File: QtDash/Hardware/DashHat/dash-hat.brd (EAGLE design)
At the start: 120.9 x 74.9 mm, 169 parts, among them IC1 LMV614, IC10 MAX9924, IC11 ZXTR2105FQ, IC2 MCP3X083008, IC3 MCP23017SS, IC4 LM358D, IC5 IL300, IC6 TSV912D, IC7 IL300, IC8 TSV912D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

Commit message: bugfix/analog-12v-input-linearity-issues: 	- added reference update after every reading -- probably not necessary 	- changed IL300 circuit values to increase drive current and opamp output voltage to deal with non-linearities in lower voltages
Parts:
- R53, R59: value 499k 1% -> 100k 1%
- R55, R61: value 10R -> 270 1%
- R56, R62: value 100k -> 20k 1%
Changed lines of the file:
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@@
 <grid distance="5" unitdist="mil" unit="mil" style="lines" multiple="1" display="yes" altdistance="1" altunitdist="mil" altunit="mil"/>
 <layers>
-<layer number="1" name="Top" color="4" fill="1" visible="yes" active="yes"/>
-<layer number="2" name="Route2" color="1" fill="3" visible="yes" active="yes"/>
+<layer number="1" name="Top" color="4" fill="1" visible="no" active="yes"/>
+<layer number="2" name="Route2" color="1" fill="3" visible="no" active="yes"/>
 <layer number="3" name="Route3" color="4" fill="3" visible="no" active="no"/>
 <layer number="4" name="Route4" color="1" fill="4" visible="no" active="no"/>
@@
 <layer number="13" name="Route13" color="4" fill="5" visible="no" active="no"/>
 <layer number="14" name="Route14" color="1" fill="6" visible="no" active="no"/>
-<layer number="15" name="Route15" color="4" fill="6" visible="yes" active="yes"/>
+<layer number="15" name="Route15" color="4" fill="6" visible="no" active="yes"/>
 <layer number="16" name="Bottom" color="9" fill="1" visible="yes" active="yes"/>
 <layer number="17" name="Pads" color="2" fill="1" visible="yes" active="yes"/>
@@
 <layer number="19" name="Unrouted" color="6" fill="1" visible="yes" active="yes"/>
 <layer number="20" name="Dimension" color="15" fill="1" visible="yes" active="yes"/>
-<layer number="21" name="tPlace" color="54" fill="1" visible="yes" active="yes"/>
-<layer number="22" name="bPlace" color="54" fill="1" visible="no" active="yes"/>
-<layer number="23" name="tOrigins" color="55" fill="1" visible="yes" active="yes"/>
-<layer number="24" name="bOrigins" color="55" fill="1" visible="no" active="yes"/>
-<layer number="25" name="tNames" color="58" fill="1" visible="yes" active="yes"/>
-<layer number="26" name="bNames" color="58" fill="1" visible="no" active="yes"/>
+<layer number="21" name="tPlace" color="54" fill="1" visible="no" active="yes"/>
+<layer number="22" name="bPlace" color="54" fill="1" visible="yes" active="yes"/>
+<layer number="23" name="tOrigins" color="55" fill="1" visible="no" active="yes"/>
+<layer number="24" name="bOrigins" color="55" fill="1" visible="yes" active="yes"/>
+<layer number="25" name="tNames" color="58" fill="1" visible="no" active="yes"/>
+<layer number="26" name="bNames" color="58" fill="1" visible="yes" active="yes"/>
 <layer number="27" name="tValues" color="7" fill="1" visible="no" active="yes"/>
-<layer number="28" name="bValues" color="7" fill="1" visible="no" active="yes"/>
-<layer number="29" name="tStop" color="7" fill="3" visible="yes" active="yes"/>
-<layer number="30" name="bStop" color="7" fill="6" visible="no" active="yes"/>
-<layer number="31" name="tCream" color="7" fill="4" visible="yes" active="yes"/>
-<layer number="32" name="bCream" color="7" fill="5" visible="no" active="yes"/>
+<layer number="28" name="bValues" color="7" fill="1" visible="yes" active="yes"/>
+<layer number="29" name="tStop" color="7" fill="3" visible="no" active="yes"/>
+<layer number="30" name="bStop" color="7" fill="6" visible="yes" active="yes"/>
+<layer number="31" name="tCream" color="7" fill="4" visible="no" active="yes"/>
+<layer number="32" name="bCream" color="7" fill="5" visible="yes" active="yes"/>
 <layer number="33" name="tFinish" color="6" fill="3" visible="no" active="yes"/>
 <layer number="34" name="bFinish" color="6" fill="6" visible="no" active="yes"/>
@@
 <layer number="37" name="tTest" color="7" fill="1" visible="no" active="yes"/>
 <layer number="38" name="bTest" color="7" fill="1" visible="no" active="yes"/>
-<layer number="39" name="tKeepout" color="4" fill="11" visible="yes" active="yes"/>
-<layer number="40" name="bKeepout" color="1" fill="11" visible="no" active="yes"/>
-<layer number="41" name="tRestrict" color="4" fill="10" visible="yes" active="yes"/>
-<layer number="42" name="bRestrict" color="1" fill="10" visible="no" active="yes"/>
+<layer number="39" name="tKeepout" color="4" fill="11" visible="no" active="yes"/>
+<layer number="40" name="bKeepout" color="1" fill="11" visible="yes" active="yes"/>
+<layer number="41" name="tRestrict" color="4" fill="10" visible="no" active="yes"/>
+<layer number="42" name="bRestrict" color="1" fill="10" visible="yes" active="yes"/>
 <layer number="43" name="vRestrict" color="2" fill="10" visible="yes" active="yes"/>
 <layer number="44" name="Drills" color="7" fill="1" visible="yes" active="yes"/>
@@
 <element name="R57" library="digital_dash" package="0603" value="100R" x="83.312" y="20.574" rot="MR0"/>
 <element name="IC5" library="digital_dash" package="DIL8-SMD" value="IL300" x="62.23" y="14.986" rot="MR0"/>
-<element name="R53" library="digital_dash" package="0603" value="499k 1%" x="69.723" y="10.414" rot="MR90"/>
-<element name="R55" library="digital_dash" package="0603" value="10R" x="70.358" y="16.256" rot="MR0"/>
-<element name="R56" library="digital_dash" package="0603" value="100k" x="52.578" y="18.288" smashed="yes" rot="MR180">
+<element name="R53" library="digital_dash" package="0603" value="100k 1%" x="69.723" y="10.414" rot="MR90"/>
+<element name="R55" library="digital_dash" package="0603" value="270 1%" x="70.358" y="16.256" rot="MR0"/>
+<element name="R56" library="digital_dash" package="0603" value="20k 1%" x="52.578" y="18.288" smashed="yes" rot="MR180">
 <attribute name="NAME" x="50.038" y="18.288" size="0.6096" layer="26" font="vector" ratio="20" rot="MR180" align="bottom-center"/>
-<attribute name="VALUE" x="49.784" y="18.542" size="0.6096" layer="28" font="vector" ratio="20" rot="MR180" align="top-center"/>
+<attribute name="VALUE" value="20k 1%" x="49.784" y="18.542" size="0.6096" layer="28" font="vector" ratio="20" rot="MR180" align="top-center"/>
 </element>
 <element name="IC6" library="digital_dash" package="SO08" value="TSV912D" x="51.308" y="23.368" smashed="yes" rot="MR90">
@@
 <attribute name="VALUE" x="82.55" y="31.242" size="0.6096" layer="28" font="vector" ratio="20" rot="MR0" align="top-center"/>
 </element>
-<element name="R59" library="digital_dash" package="0603" value="499k 1%" x="67.945" y="23.241" smashed="yes" rot="MR90">
+<element name="R59" library="digital_dash" package="0603" value="100k 1%" x="67.945" y="23.241" smashed="yes" rot="MR90">
 <attribute name="NAME" x="68.834" y="23.241" size="0.6096" layer="26" font="vector" ratio="20" rot="MR90" align="bottom-center"/>
-<attribute name="VALUE" value="499k 1%" x="67.183" y="23.241" size="0.6096" layer="28" font="vector" ratio="20" rot="MR90" align="top-center"/>
+<attribute name="VALUE" value="100k 1%" x="67.183" y="23.241" size="0.6096" layer="28" font="vector" ratio="20" rot="MR90" align="top-center"/>
 </element>
 <element name="IC7" library="digital_dash" package="DIL8-SMD" value="IL300" x="62.484" y="29.972" rot="MR0"/>
-<element name="R61" library="digital_dash" package="0603" value="10R" x="70.866" y="31.242" rot="MR0"/>
-<element name="R62" library="digital_dash" package="0603" value="100k" x="51.308" y="28.448" smashed="yes" rot="MR180">
+<element name="R61" library="digital_dash" package="0603" value="270 1%" x="70.866" y="31.242" rot="MR0"/>
+<element name="R62" library="digital_dash" package="0603" value="20k 1%" x="51.308" y="28.448" smashed="yes" rot="MR180">
 <attribute name="NAME" x="48.768" y="28.702" size="0.6096" layer="26" font="vector" ratio="20" rot="MR180" align="bottom-center"/>
-<attribute name="VALUE" x="48.514" y="27.686" size="0.6096" layer="28" font="vector" ratio="20" rot="MR180" align="top-center"/>
+<attribute name="VALUE" value="20k 1%" x="48.514" y="27.686" size="0.6096" layer="28" font="vector" ratio="20" rot="MR180" align="top-center"/>
 </element>
 <element name="IC4" library="digital_dash" package="SO08" value="LM358D" x="77.47" y="22.098" smashed="yes" rot="MR90">

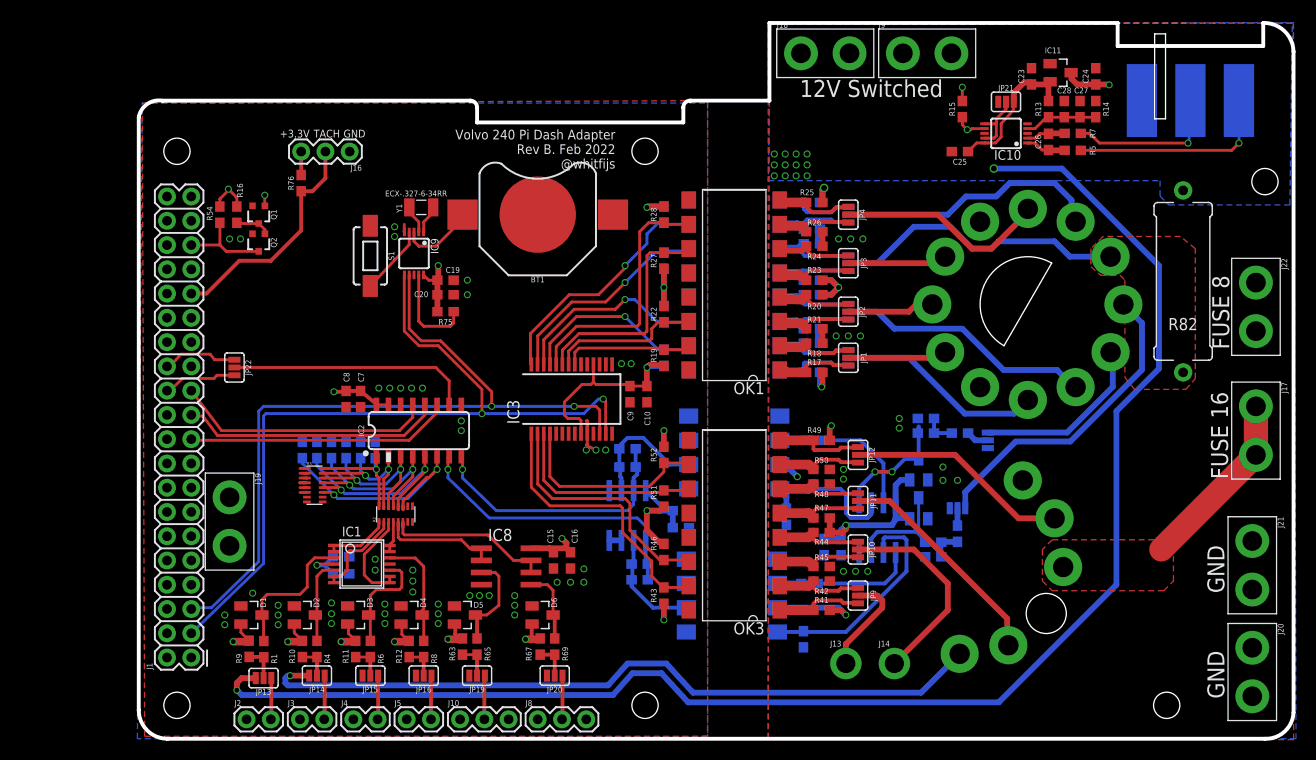
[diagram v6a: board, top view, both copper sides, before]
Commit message: topic/hardware-revc: 	- removed individual pin headers for sensor inputs -- changed to molex 8 pin for now, might be too large
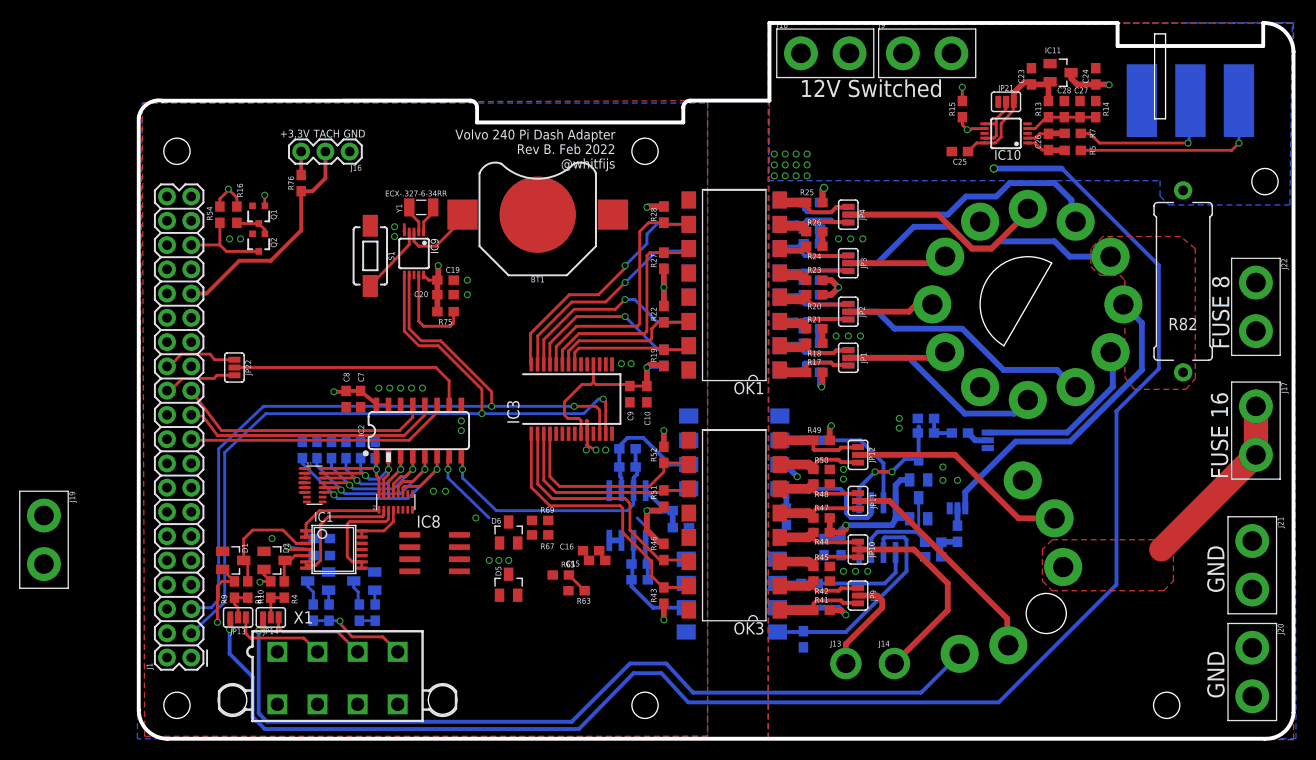
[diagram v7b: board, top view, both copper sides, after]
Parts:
- removed J10, J8: 455-1750-1-ND, SparkFun-Connectors:1X03
- removed J2, J3, J4, J5: (no value), SparkFun-Connectors:1X02
- removed JP15, JP16, JP19, JP20: JUMPER-SMT_3_NO_SILK, SparkFun-Jumpers:SMT-JUMPER_3_NO_SILK
- added X1: 5566-8, con-molex:5566-8
- moved J19 19.5 mm to (-9.78, 20.8)
- moved R69 13.3 mm to (42.2, 22.9), turned to 180 degrees
- moved R63 13.3 mm to (46.0, 15.5), turned to 180 degrees
- moved R67 11.7 mm to (42.2, 21.3), turned to 180 degrees
- moved R65 11.5 mm to (44.3, 17.1), turned to 180 degrees
- moved D6 9.34 mm to (38.9, 21.6), turned to 0 degrees
- moved JP14 7.78 mm to (14.0, 12.7)
- moved R8 7.73 mm to (23.2, 13.2), flipped to the bottom
- moved IC8 7.62 mm to (31.1, 19.4)
- moved R4 7.11 mm to (15.4, 15.6)
- moved R6 7.08 mm to (18.4, 13.2), flipped to the bottom
- moved R10 7.04 mm to (14.0, 15.6)
- moved JP13 6.89 mm to (10.5, 12.7)
- moved D2 6.54 mm to (14.4, 18.7)
- moved R1 6.46 mm to (11.6, 15.6)
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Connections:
- removed net AMBIENT_TEMP: JP20.3
- removed net MAP_SENSOR: JP19.3
- removed net N$30: JP15.2, R11.1, R6.1
- removed net N$31: JP16.2, R12.1, R8.1
- removed net N$34: JP19.2, R63.1, R65.1
- removed net N$37: JP20.2, R67.1, R69.1
- removed net OIL_PRESSURE: JP15.3
- removed net OIL_TEMP: JP16.3
- net 5V: now also X1.1; no longer J10.3, J8.3
- net GND: now also X1.8; no longer J10.1, J2.1, J3.1, J4.1, J5.1, J8.1
- net SENSOR1_IN: now also X1.2; no longer J2.2
- net SENSOR2_IN: now also X1.3; no longer J3.2
- net SENSOR3_IN: now also R11.1, R6.1, X1.4; no longer J4.2, JP15.1
- net SENSOR4_IN: now also R12.1, R8.1, X1.5; no longer J5.2, JP16.1
- net SENSOR5_IN: now also R63.1, R65.1, X1.6; no longer J10.2, JP19.1
- net SENSOR6_IN: now also R67.1, R69.1, X1.7; no longer J8.2, JP20.1
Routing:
- net N$35: track 17.7 -> 0.00 mm
- net SIG_3V3_IN1: track 30.9 -> 15.4 mm
- net 5V: track 32.9 -> 18.4 mm, vias 8 -> 3
- net N$28: track 13.0 -> 0.00 mm
- net FUEL_LVL_SENDER: track 77.9 -> 89.6 mm
- net N$29: track 10.6 -> 0.00 mm
- net N$15: track 11.9 -> 2.70 mm
- net N$11: track 11.5 -> 2.70 mm
- net COOLANT_TEMP_SENSOR: track 165.7 -> 174.3 mm
- net N$36: track 7.76 -> 0.17 mm
- net SENSOR2_IN: track 4.58 -> 10.4 mm
- net SENSOR3_IN: track 4.59 -> 10.4 mm, vias 0 -> 1
- net SENSOR1_IN: track 4.34 -> 9.99 mm
- net SENSOR6_IN: track 4.59 -> 0.00 mm
- net N$7: track 8.95 -> 4.65 mm
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
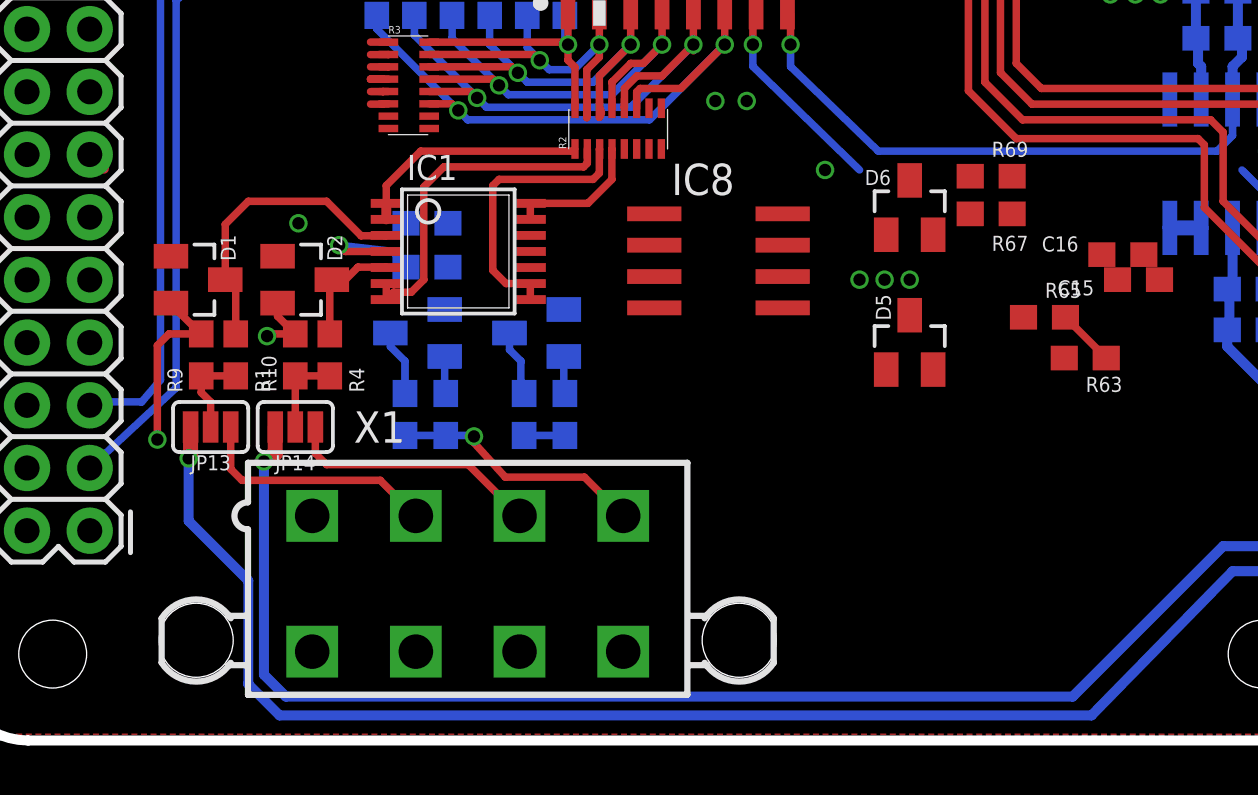
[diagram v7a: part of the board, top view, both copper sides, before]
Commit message: topic/hardware-revc: 	- replaced larger molex connector smaller molex connector
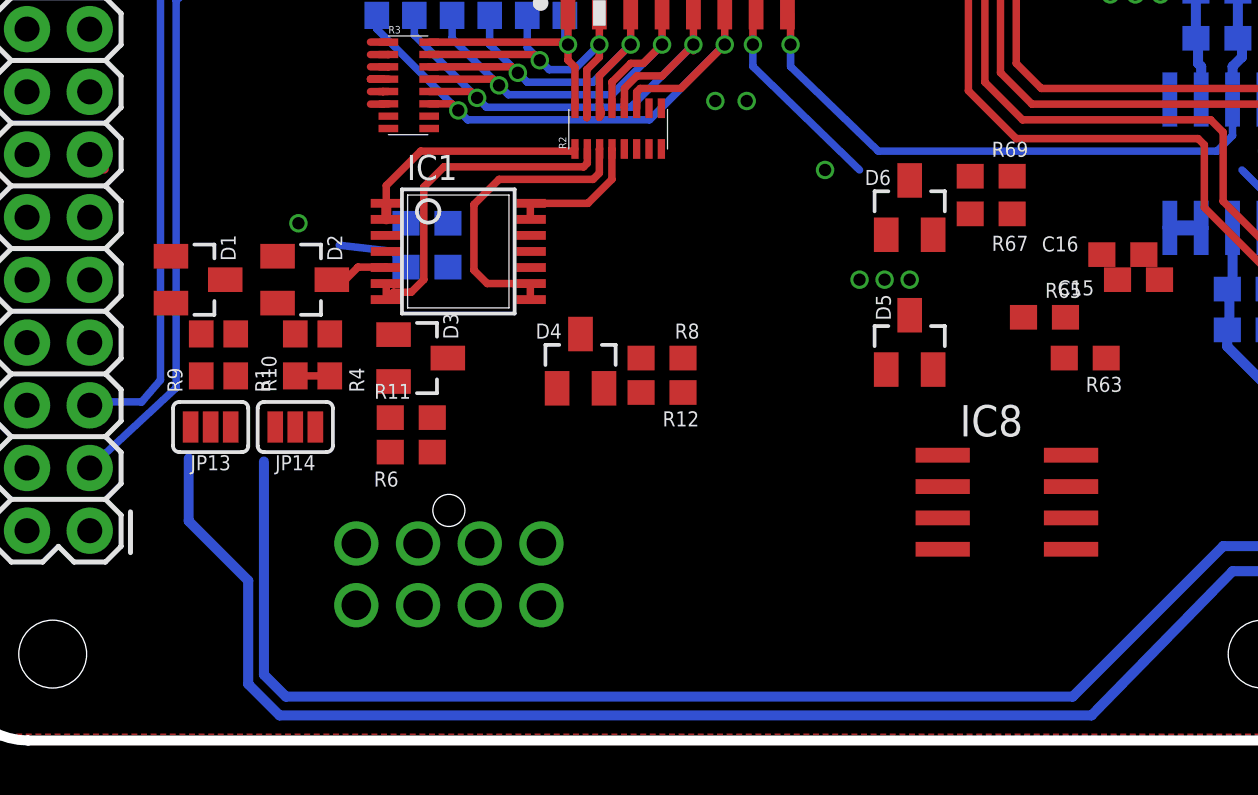
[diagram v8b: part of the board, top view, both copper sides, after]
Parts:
- removed X1: 5566-8, con-molex:5566-8
- added J2: CONN_04X2, digital_dash:MOLEX-1053102108
- moved IC8 15.2 mm to (42.8, 9.65)
- moved R8 6.04 mm to (28.8, 15.5), flipped to the top, turned to 180 degrees
- moved R12 4.04 mm to (28.8, 14.1), flipped to the top, turned to 180 degrees
- moved D4 2.11 mm to (25.5, 15.4), flipped to the top, turned to 0 degrees
- moved R6 1.55 mm to (18.7, 11.7), flipped to the top, turned to 0 degrees
- moved R11 1.40 mm to (18.7, 13.1), flipped to the top, turned to 0 degrees
- moved D3 1.02 mm to (19.1, 15.5), flipped to the top
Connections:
- net 5V: now also J2.1; no longer X1.1
- net GND: now also J2.8; no longer X1.8
- net SENSOR1_IN: now also J2.4; no longer X1.2
- net SENSOR2_IN: now also J2.3; no longer X1.3
- net SENSOR3_IN: now also J2.2; no longer X1.4
- net SENSOR4_IN: now also J2.5; no longer X1.5
- net SENSOR5_IN: now also J2.6; no longer X1.6
- net SENSOR6_IN: now also J2.7; no longer X1.7
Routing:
- net 5V: track 18.4 -> 3.27 mm, vias 3 -> 0
- net N$3: track 12.1 -> 0.00 mm
- net SENSOR2_IN: track 10.4 -> 0.00 mm
- net SENSOR3_IN: track 10.4 -> 0.00 mm, vias 1 -> 0
- net SENSOR1_IN: track 9.99 -> 0.00 mm
- net N$16: track 3.63 -> 0.00 mm
- net N$11: track 2.70 -> 0.00 mm
- net N$15: track 2.70 -> 0.00 mm
- net SENSOR5_IN: track 2.33 -> 0.00 mm
- net N$7: track 4.65 -> 2.42 mm
- net N$22: track 3.47 -> 1.40 mm
- net SENSOR4_IN: track 1.65 -> 0.00 mm
- net FUEL_LVL_SENDER: track 89.6 -> 87.9 mm, vias 1 -> 0
- net COOLANT_TEMP_SENSOR: track 174.3 -> 173.0 mm, vias 2 -> 1
- net N$9: track 11.3 -> 12.4 mm
